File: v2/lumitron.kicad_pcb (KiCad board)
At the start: 2 copper layers, 40.6 x 78.7 mm, 14 parts

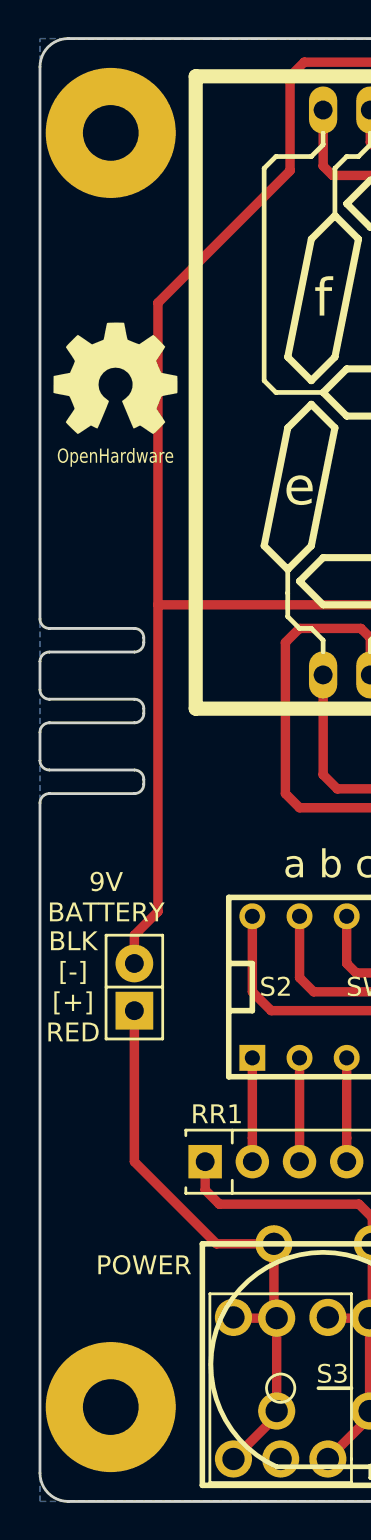
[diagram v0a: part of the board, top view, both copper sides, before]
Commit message: slots to holes, fix legend errors
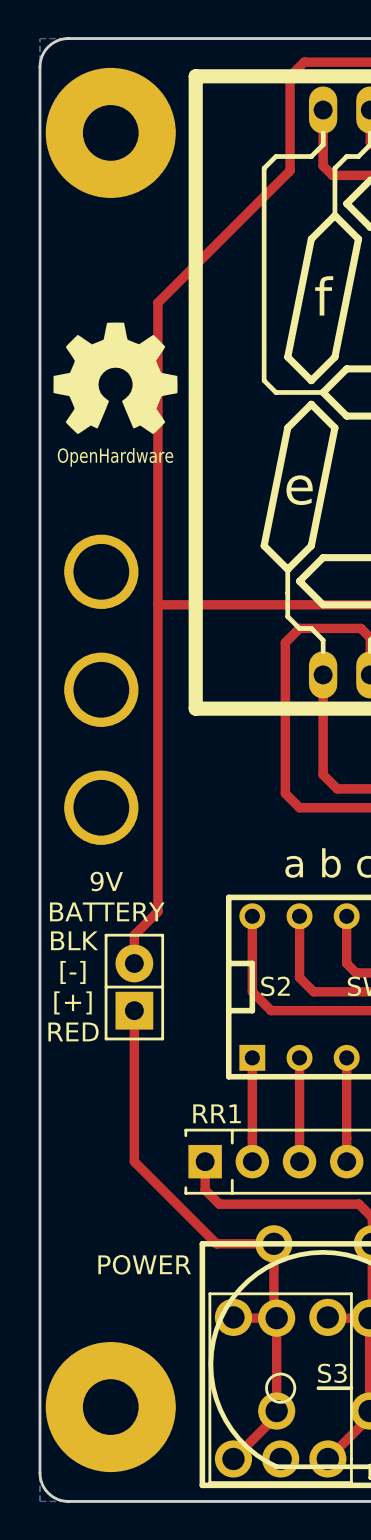
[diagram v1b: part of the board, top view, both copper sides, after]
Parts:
- added H1: MTG_H, lumitron_pcb:MountingHole_3-4mm, F.Cu at (84.6, 111.3)
- added H1: MTG_H, lumitron_pcb:MountingHole_3-4mm, F.Cu at (84.6, 104.9)
- added H1: MTG_H, lumitron_pcb:MountingHole_3-4mm, F.Cu at (84.6, 117.6)
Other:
- outline, holes or cut-outs redrawn

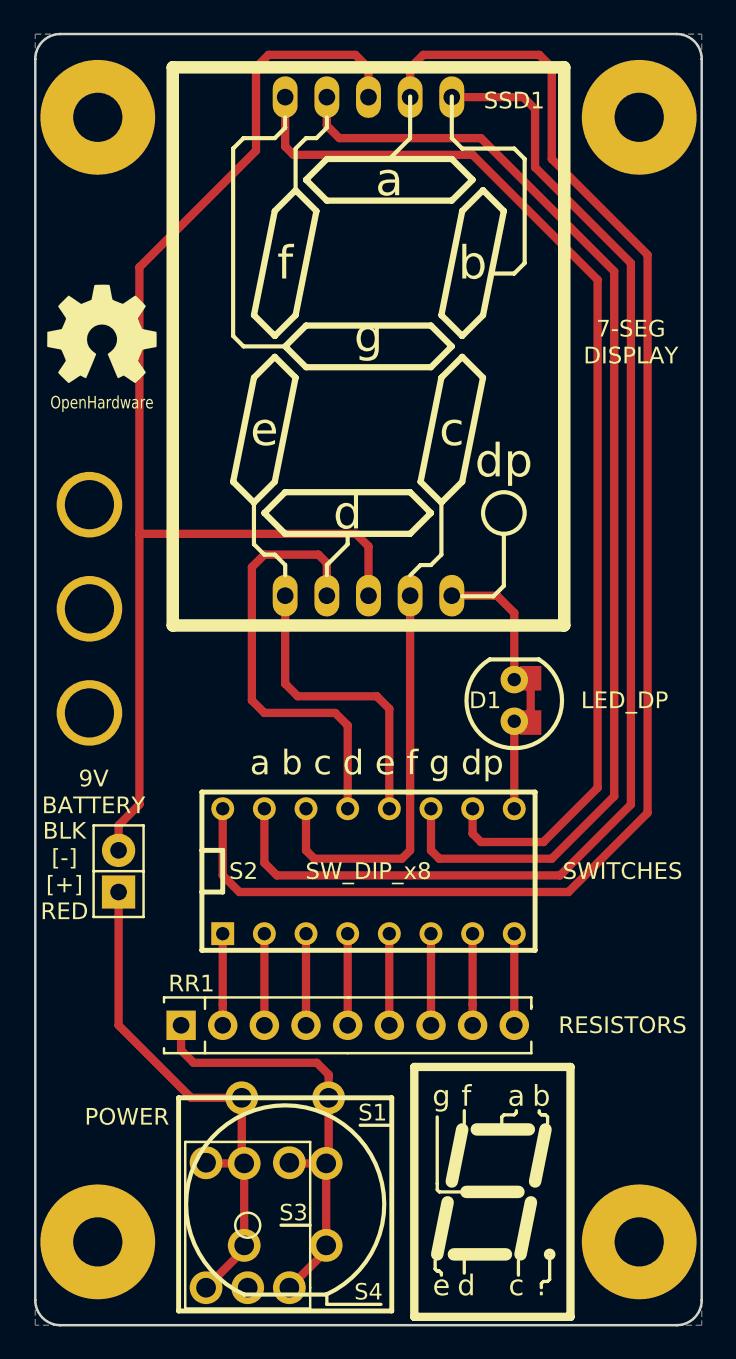
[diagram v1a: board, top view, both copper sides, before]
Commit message: added Power momentary push button
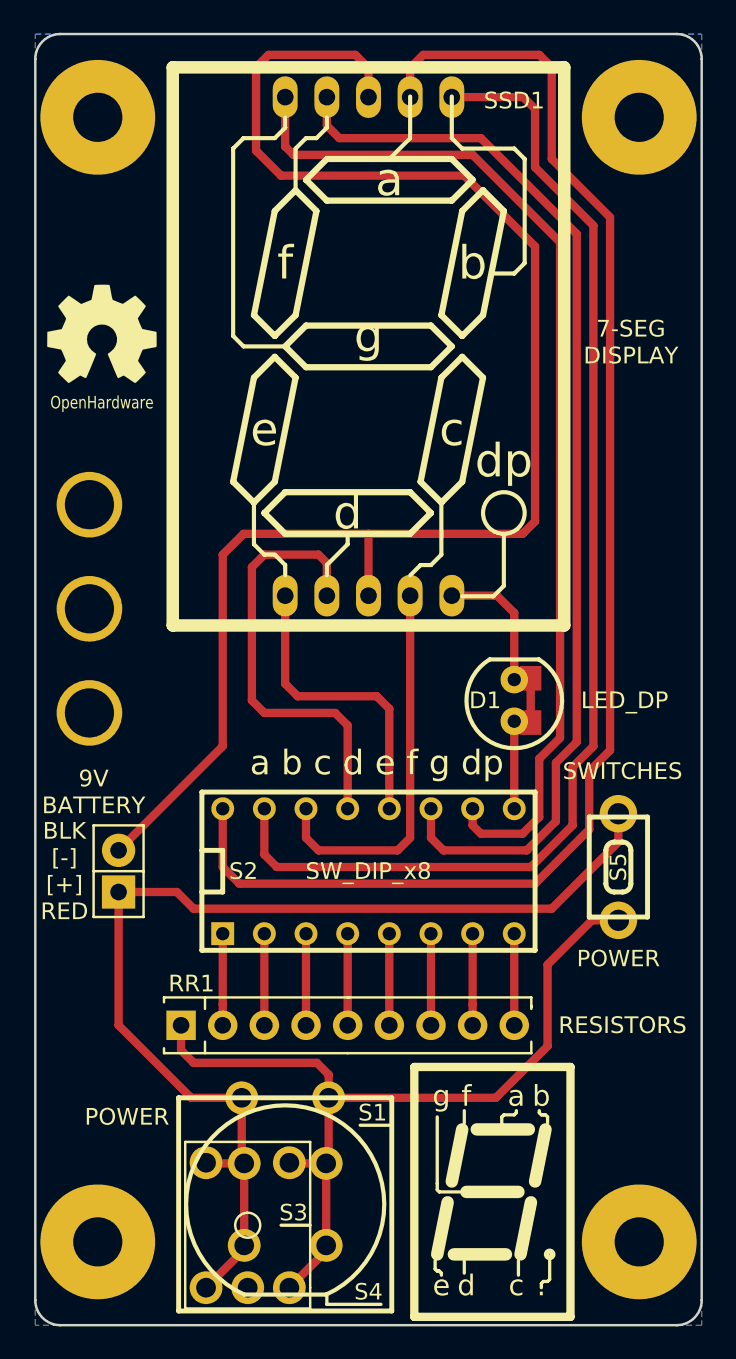
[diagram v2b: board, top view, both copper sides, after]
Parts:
- added S5: POWER, lumitron_pcb:switch_MJTP1250, F.Cu at (116.8, 127.0)
- H5, H6, H7: renamed from H1; value MTG_H -> Hole
- moved BT2 5.59 mm to (96.0, 96.8)
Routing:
- net /[+]: track 32.4 -> 66.7 mm
- net /RES: track 27.4 -> 52.5 mm
- net /[-]: track 77.8 -> 94.9 mm
- net /a: track 91.3 -> 87.2 mm
- net /f: track 70.5 -> 66.5 mm
- net /b: track 78.0 -> 74.0 mm
- net /g: track 67.1 -> 63.5 mm
- net /c: track 24.8 -> 23.5 mm
